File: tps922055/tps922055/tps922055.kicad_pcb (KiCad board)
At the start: 2 copper layers, 60 x 25 mm, 28 parts, among them J1 Conn_01x02, J2 Conn_01x05, J3 Conn_01x07, J4 Conn_01x02, U1 TPS922052DRRR

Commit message: Cheaper diode
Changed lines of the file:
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@@
 		(tags "capacitor electrolytic")
 		(property "Reference" "C6"
-			(at 0 -6.3 360)
+			(at 0 -6.3 0)
 			(layer "F.SilkS")
 			(effects
@@
 		)
 		(property "Value" "15uF"
-			(at 0 6.3 360)
+			(at 0 6.3 0)
 			(layer "F.Fab")
 			(effects
@@
 		)
 		(fp_text user "${REFERENCE}"
-			(at 0 0 360)
+			(at 0 0 0)
 			(layer "F.Fab")
 			(effects
@@
 		(tags "capacitor")
 		(property "Reference" "C5"
-			(at -2.575 0 360)
+			(at -2.575 0 0)
 			(layer "F.SilkS")
 			(effects
@@
 		)
 		(property "Value" "1uF"
-			(at 0 1.43 360)
+			(at 0 1.43 0)
 			(layer "F.Fab")
 			(effects
@@
 		)
 		(fp_text user "${REFERENCE}"
-			(at 0 0 360)
+			(at 0 0 0)
 			(layer "F.Fab")
 			(effects
@@
 		(at 178.2 83.4 90)
 		(property "Reference" "J1"
-			(at 0 -0.780001 270)
+			(at 0 -0.780001 -90)
 			(layer "F.SilkS")
 			(effects
@@
 		)
 		(property "Value" "Conn_01x02"
-			(at 0 -9.799999 270)
+			(at 0 -9.799999 -90)
 			(layer "F.Fab")
 			(effects
@@
 		)
 		(property "Footprint" "MHCI:2060-452-998-404 Wago"
-			(at 0 0 270)
+			(at 0 0 -90)
 			(layer "F.Fab")
 			(hide yes)
@@
 		)
 		(property "Datasheet" ""
-			(at 0 0 270)
+			(at 0 0 -90)
 			(layer "F.Fab")
 			(hide yes)
@@
 		)
 		(property "Description" "Generic connector, single row, 01x02, script generated (kicad-library-utils/schlib/autogen/connector/)"
-			(at 0 0 270)
+			(at 0 0 -90)
 			(layer "F.Fab")
 			(hide yes)
@@
 		)
 		(fp_text user "Copyright 2016 Accelerated Designs. All rights reserved."
-			(at 0 0 270)
+			(at 0 0 -90)
 			(layer "Cmts.User")
 			(effects
@@
 			)
 		)
-		(property "LCSC" "C145187"
+		(property "LCSC" "C151733"
+			(at 0 0 -90)
+			(unlocked yes)
+			(layer "F.Fab")
+			(hide yes)
+			(effects
+				(font
+					(size 1 1)
+					(thickness 0.15)
+				)
+			)
+		)
+		(property "LCSC_Alt" "C145187"
 			(at 0 0 -90)
 			(unlocked yes)
@@
 			(size 1.125 1.75)
 			(layers "F.Cu" "F.Paste" "F.Mask")
-			(roundrect_rratio 0.222222)
+			(roundrect_rratio 0.2222222222)
 			(net 11 "/CSN")
 			(pintype "passive")
@@
 			(size 1.125 1.75)
 			(layers "F.Cu" "F.Paste" "F.Mask")
-			(roundrect_rratio 0.222222)
+			(roundrect_rratio 0.2222222222)
 			(net 1 "LED-")
 			(pintype "passive")
@@
 		(tags "solder jumper open")
 		(property "Reference" "JP1"
-			(at 0 1.8 360)
+			(at 0 1.8 0)
 			(layer "B.SilkS")
 			(effects
@@
 		)
 		(property "Value" "Jumper_3_Open"
-			(at 0 -1.9 360)
+			(at 0 -1.9 0)
 			(layer "B.Fab")
 			(effects
@@
 		(tags "Through hole pin header THT 1x05 2.54mm single row")
 		(property "Reference" "J2"
-			(at 0 2.33 270)
+			(at 0 2.33 -90)
 			(layer "B.SilkS")
 			(effects
@@
 		)
 		(property "Value" "Conn_01x05"
-			(at 0 -12.49 270)
+			(at 0 -12.49 -90)
 			(layer "B.Fab")
 			(effects

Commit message: Schematic needs vias
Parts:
- removed JP3: Jumper_2_Open, Jumper:SolderJumper-2_P1.3mm_Open_RoundedPad1.0x1.5mm
- moved C7 8.42 mm to (166.3, 83.5)
- moved C3 8.35 mm to (168.2, 83.5)
- moved R3 5.30 mm to (163.1, 103.0), turned to 180 degrees
- moved HS1 4.72 mm to (161.8, 93.5)
- moved D1 3.69 mm to (157.5, 87.6)
- moved L1 3.54 mm to (164.8, 90.9)
- moved C1 3.00 mm to (163.1, 101.5), turned to 180 degrees
- moved R8 2.67 mm to (170.9, 93.7), turned to 0 degrees
- moved C6 1.22 mm to (143.8, 89.4)
- moved C4 0.85 mm to (153.6, 95.5)
- moved R1 0.85 mm to (153.6, 98.7)
- moved R5 0.85 mm to (169.9, 101.5)
- moved R7 0.85 mm to (164.7, 97.5)
- moved C2 0.85 mm to (162.3, 96.7)
- moved C5 0.85 mm to (153.6, 97.0)
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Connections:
- C5 pad 2: LED+ -> /VCC
- U1 pad 2: LED+ -> /VCC
- U1 pad 5: FAULT -> GND
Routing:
- net LED+: track 0.00 -> 62.4 mm
- net EN: track 3.14 -> 24.8 mm, vias 0 -> 1
- net LED-: track 0.00 -> 18.6 mm
- net ADIM: track 3.04 -> 21.2 mm, vias 0 -> 1
- net /UVP: track 0.00 -> 13.0 mm
- net /CSN: track 0.00 -> 12.0 mm
- net /CSP: track 0.00 -> 4.81 mm
- net /COMP: track 0.00 -> 3.78 mm
- net /COMP2: track 0.00 -> 3.32 mm
- net /VCC: track 0.00 -> 2.48 mm
- net /TEMP: track 0.00 -> 2.27 mm
- net /FSET: track 0.00 -> 2.04 mm
- net /SW: track 0.00 -> 1.80 mm
- net GND: vias 28 -> 37
- added copper zone on F.Cu, net /CSN
- added copper zone on F.Cu, net /SW
- added copper zone on F.Cu, net LED+
- added copper zone on F.Cu, net LED-

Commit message: TPS Layout complete
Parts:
- removed D1: D, Diode_SMD:D_SMC
- added D2: D_Schottky, Diode_SMD:D_SMC, F.Cu at (157.9, 87.6)
- added JP5: Jumper_3_Open, Jumper:SolderJumper-3_P1.3mm_Open_RoundedPad1.0x1.5mm, B.Cu at (159.6, 100.8)
- added R10: 56k, Resistor_SMD:R_0603_1608Metric, F.Cu at (158.8, 99.8)
- C7: value 0.1uF -> 100nF
- R1: value R_US -> 56k
- R2: value R_US -> 27k
- moved C1 1.05 mm to (164.0, 100.9)
- moved R3 1.05 mm to (164.0, 102.5)
- moved R4 1.05 mm to (164.0, 99.2)
- moved R2 0.74 mm to (160.4, 99.8)
- moved R1 0.55 mm to (153.6, 98.1)
- moved R8 0.55 mm to (170.9, 93.1)
- moved C2 0.55 mm to (162.3, 96.1)
- moved C4 0.55 mm to (153.6, 94.9)
- moved C5 0.55 mm to (153.6, 96.5)
- moved R5 0.55 mm to (169.9, 100.9)
- moved R6 0.55 mm to (170.0, 97.7)
- moved R7 0.55 mm to (164.7, 96.9)
- moved U1 0.55 mm to (157.9, 96.5)
- moved C7 0.50 mm to (165.8, 83.5)
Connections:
- R2 pad 2: GND -> Net-(JP5-A)
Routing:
- net Net-(JP5-A): track 0.00 -> 3.13 mm, vias 0 -> 1
- net Net-(JP5-B): track 0.00 -> 2.97 mm, vias 0 -> 1
- net GND: track 0.00 -> 1.63 mm, vias 37 -> 72
- net /FSET: track 2.04 -> 3.66 mm
- net LED-: track 18.6 -> 19.7 mm
- net /COMP: track 3.78 -> 4.68 mm
- net /CSN: track 12.0 -> 11.2 mm
- net LED+: track 62.4 -> 61.9 mm
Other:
- board text added: "400kHz"
- board text added: "800kHz"

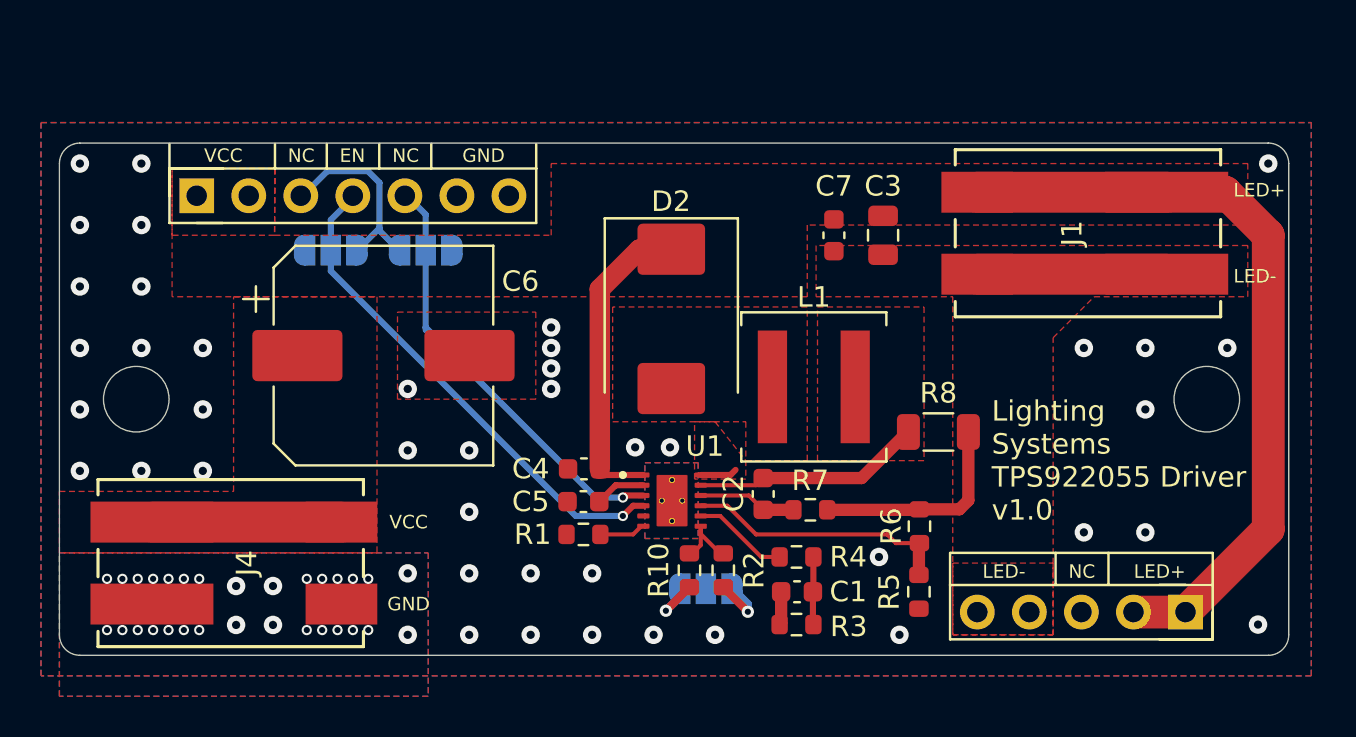
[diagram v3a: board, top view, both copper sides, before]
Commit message: TPS922052 - Larger inductor
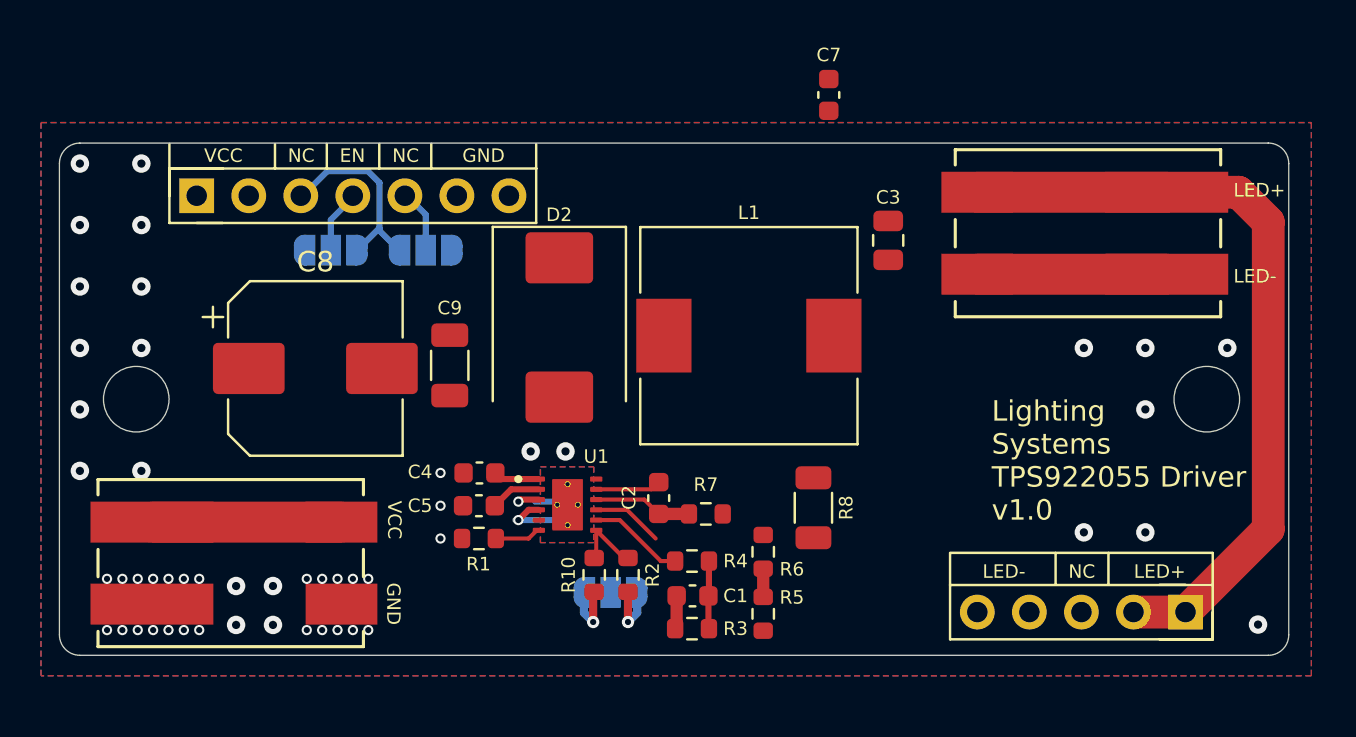
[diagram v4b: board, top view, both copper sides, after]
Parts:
- removed C6: 15uF, Capacitor_SMD:CP_Elec_10x10.5
- added C8: 47uF, Capacitor_SMD:CP_Elec_8x10, F.Cu at (140.5, 90.0)
- added C9: 4.7uF, Capacitor_SMD:C_1206_3216Metric, F.Cu at (147.1, 89.8)
- L1: value 10uH -> 22uH; footprint Inductor_SMD:L_Coilcraft_XAL6060-XXX -> Inductor_SMD:L_10.4x10.4_H4.8
- moved HS1 54.3 mm to (129.6, 49.8)
- moved R6 7.73 mm to (162.3, 99.0)
- moved R5 7.68 mm to (162.3, 102.0)
- moved R8 7.13 mm to (164.8, 96.8), turned to -90 degrees
- moved C7 6.85 mm to (165.6, 76.7)
- moved D2 5.48 mm to (152.4, 88.0)
- moved C1 5.10 mm to (158.9, 101.1)
- moved C2 5.10 mm to (157.2, 96.3)
- moved C4 5.10 mm to (148.5, 95.1)
- moved C5 5.10 mm to (148.5, 96.7)
- moved R1 5.10 mm to (148.5, 98.3)
- moved R3 5.10 mm to (158.9, 102.7)
- moved R4 5.10 mm to (158.9, 99.4)
- moved R7 5.10 mm to (159.6, 97.1)
- moved U1 5.10 mm to (152.8, 96.7)
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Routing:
- net EN: track 24.6 -> 6.65 mm
- net ADIM: track 21.0 -> 4.08 mm
- net LED+: track 61.9 -> 49.6 mm
- net LED-: track 19.7 -> 9.25 mm
- net /UVP: track 13.0 -> 4.85 mm
- net /CSN: track 11.2 -> 3.50 mm
- net /SW: track 1.80 -> 0.00 mm
- net GND: track 1.63 -> 2.95 mm, vias 72 -> 51
- removed copper zone on F.Cu, net /CSN
- removed copper zone on F.Cu, net /SW
- removed copper zone on F.Cu, net LED+
- removed copper zone on F.Cu, net LED-

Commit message: TPS922052 v1.0
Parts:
- added JP3: Jumper_2_Open, Jumper:SolderJumper-2_P1.3mm_Open_RoundedPad1.0x1.5mm, F.Cu at (167.8, 87.3)
- R1: value 56k -> 27k
- moved HS1 50.9 mm to (156.5, 93.0)
- moved C7 7.14 mm to (166.7, 83.7)
- moved R8 6.00 mm to (168.4, 92.0), turned to 0 degrees
- moved R3 3.37 mm to (160.4, 99.7), turned to -90 degrees
- moved C9 2.95 mm to (146.3, 87.0)
- moved R6 2.29 mm to (162.1, 96.7)
- moved R5 2.29 mm to (162.1, 99.7)
- moved C8 2.20 mm to (139.8, 87.9)
- moved R4 1.80 mm to (157.1, 99.7), turned to 90 degrees
- moved L1 1.55 mm to (160.1, 88.5)
- moved C1 1.43 mm to (158.8, 99.7), turned to -90 degrees
- moved D2 1.40 mm to (151.0, 88.0)
- moved R7 0.83 mm to (159.1, 96.4)
- moved C2 0.77 mm to (156.8, 95.7)
- moved JP5 0.46 mm to (154.6, 100.6)
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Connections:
- C3 pad 2: LED- -> /OUTCAP
- C7 pad 2: LED- -> /OUTCAP
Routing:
- net LED+: track 49.6 -> 67.3 mm
- net LED-: track 9.25 -> 25.2 mm
- net ADIM: track 4.08 -> 19.1 mm
- net EN: track 6.65 -> 20.9 mm
- net /CSN: track 3.50 -> 15.6 mm
- net /UVP: track 4.85 -> 10.00 mm
- net /SW: track 0.00 -> 2.98 mm
- net /COMP: track 4.68 -> 5.47 mm
- net GND: track 2.95 -> 3.34 mm, vias 51 -> 75
- added copper zone on F.Cu, net /CSN
- added copper zone on F.Cu, net /OUTCAP
- added copper zone on F.Cu, net /SW
- added copper zone on F.Cu, net LED+
- added copper zone on F.Cu, net LED-
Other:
- board text added: "Cout"
